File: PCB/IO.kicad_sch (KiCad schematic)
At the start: 39 parts, among them J501 Conn_02x03_Counter_Clockwise, J502 USB_C_Receptacle_USB2.0_16P, J503 Screw_Terminal_01x06, J504 Screw_Terminal_01x04, J505 Conn_01x04, J506 Conn_02x03_Counter_Clockwise, J507 Conn_01x06, J508 VCC, Q1 SL2302S, SW1 SW_Push, SW2 SW_Push

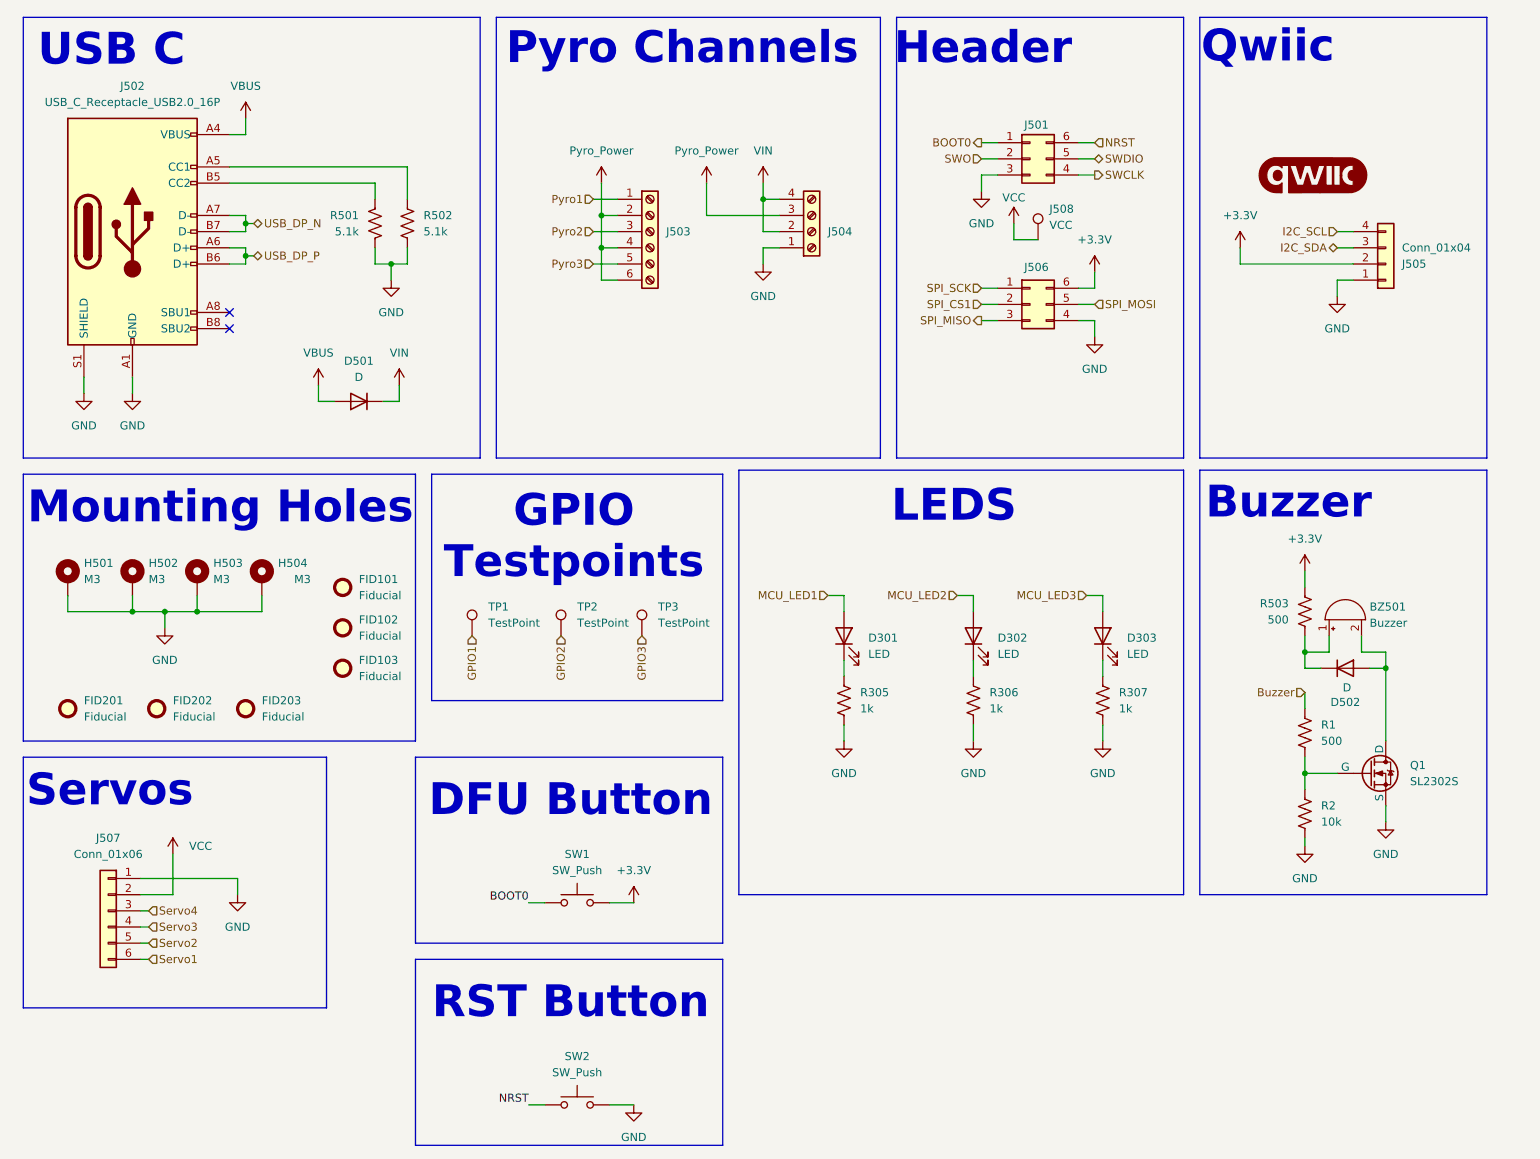
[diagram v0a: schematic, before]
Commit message: - Swapped out 2 LED's for neopixels- Added reverse polarity protection- Replaced Radio module with deticated IC and passives
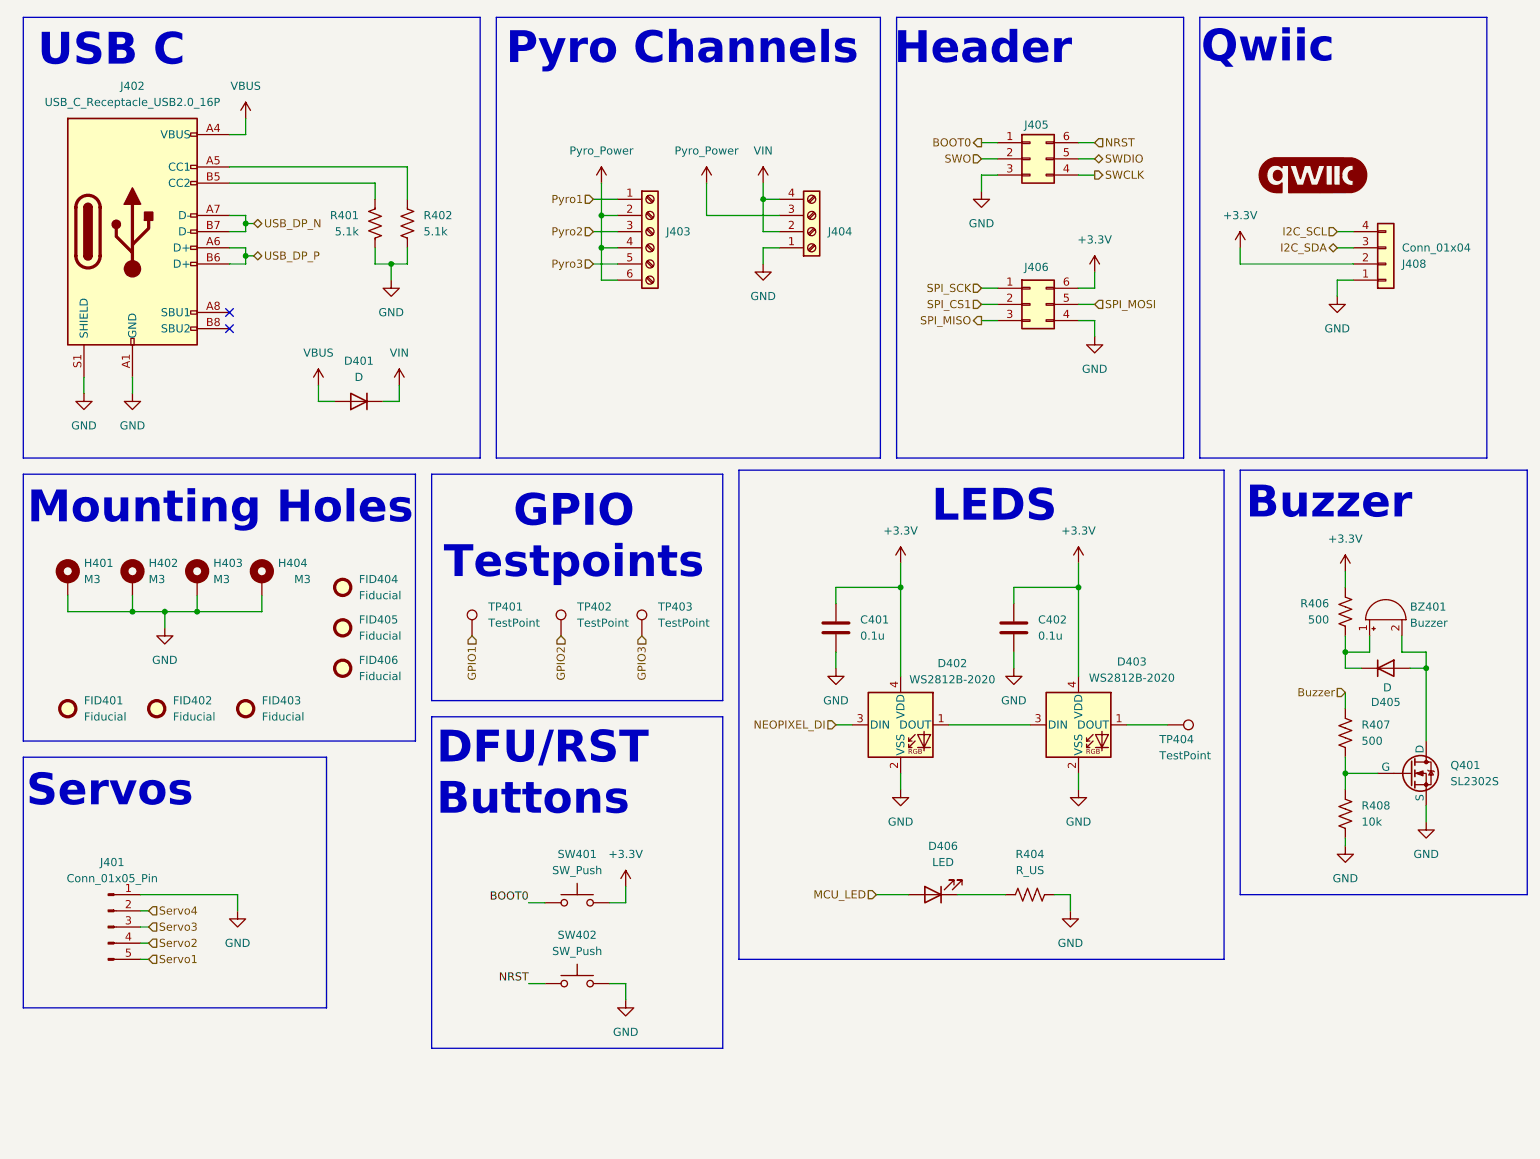
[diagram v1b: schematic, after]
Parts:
- removed D301, D302, D303: LED, LED_SMD:LED_0603_1608Metric_Pad1.05x0.95mm_HandSolder, symbol Device:LED
- removed J507: Conn_01x06, Connector_PinHeader_2.54mm:PinHeader_1x06_P2.54mm_Vertical, symbol Connector_Generic:Conn_01x06
- removed J508: VCC, TestPoint:TestPoint_Pad_1.0x1.0mm, symbol Connector:TestPoint
- removed R305, R306, R307: 1k, Resistor_SMD:R_0603_1608Metric_Pad0.98x0.95mm_HandSolder, symbol Device:R_US
- added C401, C402: 0.1u, Capacitor_SMD:C_0603_1608Metric_Pad1.08x0.95mm_HandSolder, symbol Device:C
- added D402, D403: WS2812B-2020, LED_SMD:LED_WS2812B-2020_PLCC4_2.0x2.0mm, symbol LED:WS2812B-2020
- added D406: LED, LED_SMD:LED_0603_1608Metric_Pad1.05x0.95mm_HandSolder, symbol Device:LED
- added J401: Conn_01x05_Pin, Connector_PinHeader_2.54mm:PinHeader_1x05_P2.54mm_Vertical, symbol Connector:Conn_01x05_Pin
- added R404: R_US, Resistor_SMD:R_0603_1608Metric_Pad0.98x0.95mm_HandSolder, symbol Device:R_US
- added TP404: TestPoint, TestPoint:TestPoint_Pad_D1.5mm, symbol Connector:TestPoint
- renumbered BZ501 to BZ401, D501 to D401, D502 to D405, FID201 to FID401, FID202 to FID402, FID203 to FID403, FID101 to FID404, FID102 to FID405, FID103 to FID406, G501 to G401, H501 to H401, H502 to H402, H503 to H403, H504 to H404, J502 to J402, J503 to J403, J504 to J404, J501 to J405, J506 to J406, J505 to J408, Q1 to Q401, R501 to R401, R502 to R402, R503 to R406, R1 to R407, R2 to R408, SW1 to SW401, SW2 to SW402, TP1 to TP401, TP2 to TP402, TP3 to TP403
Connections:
- net +3.3V: now also C401.1, C402.1, D402.4 (VDD), D403.4 (VDD)
- net GND: now also C401.2, C402.2, D402.2 (VSS), D403.2 (VSS), J401.1 (Pin_1), R404.2
- net Servo1: now also J401.5 (Pin_5)
- net Servo2: now also J401.4 (Pin_4)
- net Servo3: now also J401.3 (Pin_3)
- net Servo4: now also J401.2 (Pin_2)
- new net: D406.1 (K), R404.1
- new net: D402.1 (DOUT), D403.3 (DIN)
- new net: D403.1 (DOUT), TP404.1
- new net MCU_LED: D406.2 (A)
- new net NEOPIXEL_DI: D402.3 (DIN)
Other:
- note added: "DFU/RST Buttons"
- note removed: "DFU Button"
- note removed: "RST Button"
- moved on the sheet: BZ401, D405, Q401, R406, R407, R408, SW402

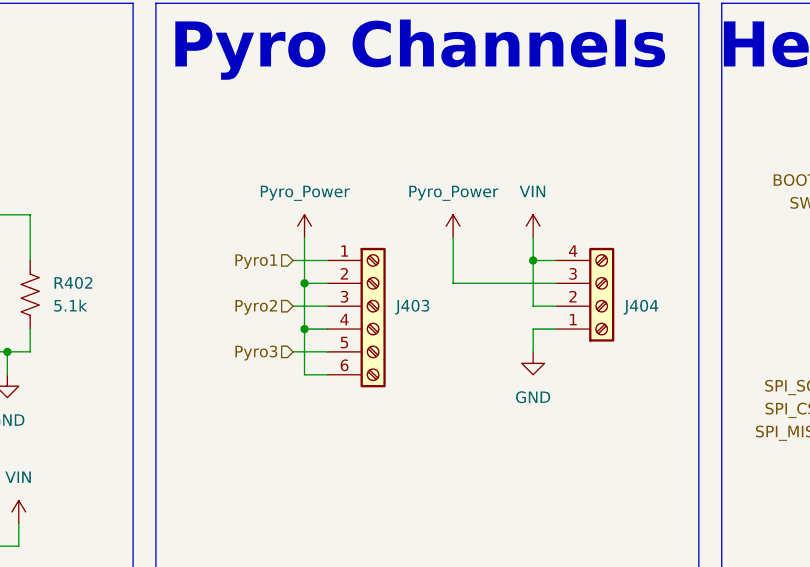
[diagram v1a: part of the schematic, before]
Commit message: Updated PCB to have the new parts (unrouted)
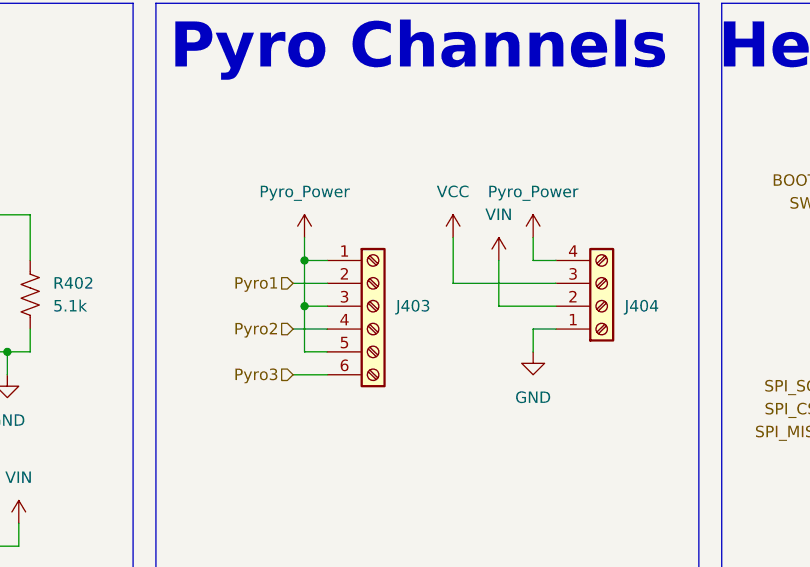
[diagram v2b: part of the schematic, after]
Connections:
- net +3.3V: now also SW401.3, SW401.4; no longer SW401.2
- net BOOT0: now also SW401.2
- net GND: now also SW402.3, SW402.4; no longer SW402.2
- net NRST: now also SW402.2
- net Pyro1: now also J403.2 (Pin_2); no longer J403.1 (Pin_1)
- net Pyro2: now also J403.4 (Pin_4); no longer J403.3 (Pin_3)
- net Pyro3: now also J403.6 (Pin_6); no longer J403.5 (Pin_5)
- net Pyro_Power: now also J403.1 (Pin_1), J403.3 (Pin_3), J403.5 (Pin_5), J404.4 (Pin_4); no longer J403.2 (Pin_2), J403.4 (Pin_4), J403.6 (Pin_6), J404.3 (Pin_3)
- net VIN: no longer J404.4 (Pin_4)
- new net VCC: J404.3 (Pin_3)
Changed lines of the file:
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@@
 	)
 	(junction
-		(at 105.41 50.8)
+		(at 105.41 48.26)
 		(diameter 0)
 		(color 0 0 0 0)
@@
 	)
 	(junction
-		(at 105.41 45.72)
-		(diameter 0)
-		(color 0 0 0 0)
-	)
-	(junction
 		(at 234.95 116.84)
 		(diameter 0)
@@
 	)
 	(junction
-		(at 130.81 43.18)
+		(at 72.39 53.34)
 		(diameter 0)
 		(color 0 0 0 0)
 	)
 	(junction
-		(at 72.39 53.34)
+		(at 105.41 43.18)
 		(diameter 0)
 		(color 0 0 0 0)
@@
 	(wire
 		(pts
-			(xy 104.14 53.34) (xy 107.95 53.34)
-		)
-		(stroke
-			(width 0)
-			(type default)
-		)
-	)
-	(wire
-		(pts
 			(xy 60.96 74.93) (xy 63.5 74.93)
 		)
@@
 	(wire
 		(pts
-			(xy 107.95 55.88) (xy 105.41 55.88)
+			(xy 234.95 114.3) (xy 234.95 116.84)
 		)
 		(stroke
@@
 	(wire
 		(pts
-			(xy 234.95 114.3) (xy 234.95 116.84)
+			(xy 104.14 55.88) (xy 107.95 55.88)
 		)
 		(stroke
@@
 	(wire
 		(pts
-			(xy 133.35 48.26) (xy 130.81 48.26)
+			(xy 220.98 58.42) (xy 220.98 55.88)
 		)
 		(stroke
@@
 	(wire
 		(pts
-			(xy 220.98 58.42) (xy 220.98 55.88)
+			(xy 165.1 39.37) (xy 167.64 39.37)
 		)
 		(stroke
@@
 	(wire
 		(pts
-			(xy 165.1 39.37) (xy 167.64 39.37)
+			(xy 21.59 107.95) (xy 21.59 105.41)
 		)
 		(stroke
@@
 	(wire
 		(pts
-			(xy 21.59 107.95) (xy 21.59 105.41)
+			(xy 142.24 104.14) (xy 152.4 104.14)
 		)
 		(stroke
@@
 	(wire
 		(pts
-			(xy 142.24 104.14) (xy 152.4 104.14)
+			(xy 182.88 36.83) (xy 180.34 36.83)
 		)
 		(stroke
@@
 	(wire
 		(pts
-			(xy 182.88 36.83) (xy 180.34 36.83)
+			(xy 105.41 40.64) (xy 105.41 43.18)
 		)
 		(stroke
@@
 	(wire
 		(pts
-			(xy 105.41 50.8) (xy 105.41 45.72)
+			(xy 127 48.26) (xy 133.35 48.26)
 		)
 		(stroke
@@
 	(wire
 		(pts
-			(xy 105.41 55.88) (xy 105.41 50.8)
+			(xy 107.95 53.34) (xy 105.41 53.34)
 		)
 		(stroke
@@
 	(wire
 		(pts
-			(xy 130.81 48.26) (xy 130.81 43.18)
+			(xy 142.24 104.14) (xy 142.24 106.68)
 		)
 		(stroke
@@
 	(wire
 		(pts
-			(xy 142.24 104.14) (xy 142.24 106.68)
+			(xy 222.25 133.35) (xy 222.25 135.89)
 		)
 		(stroke
@@
 	(wire
 		(pts
-			(xy 222.25 133.35) (xy 222.25 135.89)
+			(xy 72.39 55.88) (xy 72.39 53.34)
 		)
 		(stroke
@@
 	(wire
 		(pts
-			(xy 72.39 55.88) (xy 72.39 53.34)
+			(xy 105.41 48.26) (xy 105.41 53.34)
 		)
 		(stroke
@@
 	(wire
 		(pts
-			(xy 104.14 43.18) (xy 107.95 43.18)
-		)
-		(stroke
-			(width 0)
-			(type default)
-		)
-	)
-	(wire
-		(pts
 			(xy 222.25 144.78) (xy 222.25 143.51)
 		)
@@
 	(wire
 		(pts
-			(xy 105.41 45.72) (xy 107.95 45.72)
+			(xy 105.41 43.18) (xy 107.95 43.18)
 		)
 		(stroke
@@
 	(wire
 		(pts
+			(xy 105.41 48.26) (xy 107.95 48.26)
+		)
+		(stroke
+			(width 0)
+			(type default)
+		)
+	)
+	(wire
+		(pts
 			(xy 36.83 107.95) (xy 41.91 107.95)
 		)
@@
 	(wire
 		(pts
-			(xy 105.41 45.72) (xy 105.41 40.64)
+			(xy 142.24 125.73) (xy 144.78 125.73)
 		)
 		(stroke
@@
 	(wire
 		(pts
-			(xy 142.24 125.73) (xy 144.78 125.73)
+			(xy 121.92 45.72) (xy 133.35 45.72)
 		)
 		(stroke
@@
 	(wire
 		(pts
-			(xy 121.92 45.72) (xy 133.35 45.72)
+			(xy 104.14 50.8) (xy 107.95 50.8)
 		)
 		(stroke
@@
 	(wire
 		(pts
-			(xy 104.14 48.26) (xy 107.95 48.26)
+			(xy 127 43.18) (xy 127 48.26)
 		)
 		(stroke
@@
 	(wire
 		(pts
-			(xy 105.41 50.8) (xy 107.95 50.8)
-		)
-		(stroke
-			(width 0)
-			(type default)
-		)
-	)
-	(wire
-		(pts
 			(xy 180.34 62.23) (xy 182.88 62.23)
 		)
@@
 	(wire
 		(pts
+			(xy 104.14 45.72) (xy 107.95 45.72)
+		)
+		(stroke
+			(width 0)
+			(type default)
+		)
+	)
+	(wire
+		(pts
+			(xy 105.41 43.18) (xy 105.41 48.26)
+		)
+		(stroke
+			(width 0)
+			(type default)
+		)
+	)
+	(wire
+		(pts
 			(xy 33.02 162.56) (xy 34.29 162.56)
 		)
@@
 		)
 	)
-	(hierarchical_label "Pyro2"
-		(shape input)
-		(at 104.14 48.26 180)
-		(effects
-			(font
-				(size 1.27 1.27)
-			)
-			(justify right)
-		)
-	)
 	(hierarchical_label "GPIO2"
 		(shape input)
@@
 		)
 	)
-	(hierarchical_label "Pyro1"
+	(hierarchical_label "Pyro2"
 		(shape input)
-		(at 104.14 43.18 180)
+		(at 104.14 50.8 180)
 		(effects
 			(font
@@
 		)
 	)
+	(hierarchical_label "Pyro1"
+		(shape input)
+		(at 104.14 45.72 180)
+		(effects
+			(font
+				(size 1.27 1.27)
+			)
+			(justify right)
+		)
+	)
 	(hierarchical_label "BOOT0"
 		(shape output)
@@
 		)
 	)
+	(hierarchical_label "Pyro3"
+		(shape input)
+		(at 104.14 55.88 180)
+		(effects
+			(font
+				(size 1.27 1.27)
+			)
+			(justify right)
+		)
+	)
 	(hierarchical_label "SWCLK"
 		(shape output)
@@
 		)
 	)
-	(hierarchical_label "Pyro3"
-		(shape input)
-		(at 104.14 53.34 180)
-		(effects
-			(font
-				(size 1.27 1.27)
-			)
-			(justify right)
-		)
-	)
 	(symbol
 		(lib_id "Connector_Generic:Conn_02x03_Counter_Clockwise")
@@
 			)
 		)
-		(property "Value" "Pyro_Power"
+		(property "Value" "VCC"
 			(at 121.92 35.56 0)
 			(show_name no)
@@
 			)
 		)
-		(property "Value" "VIN"
+		(property "Value" "Pyro_Power"
 			(at 130.81 35.56 0)
 			(show_name no)
@@
 	)
 	(symbol
+		(lib_id "power:VBUS")
+		(at 127 43.18 0)
+		(unit 1)
+		(body_style 1)
+		(exclude_from_sim no)
+		(in_bom yes)
+		(on_board yes)
+		(in_pos_files yes)
+		(dnp no)
+		(fields_autoplaced yes)
+		(property "Reference" "#PWR0429"
+			(at 127 46.99 0)
+			(hide yes)
+			(show_name no)
+			(do_not_autoplace no)
+			(effects
+				(font
+					(size 1.27 1.27)
+				)
+			)
+		)
+		(property "Value" "VIN"
+			(at 127 38.1 0)
+			(show_name no)
+			(do_not_autoplace no)
+			(effects
+				(font
+					(size 1.27 1.27)
+				)
+			)
+		)
+		(property "Footprint" ""
+			(at 127 43.18 0)
+			(hide yes)
+			(show_name no)
+			(do_not_autoplace no)
+			(effects
+				(font
+					(size 1.27 1.27)
+				)
+			)
+		)
+		(property "Datasheet" ""
+			(at 127 43.18 0)
+			(hide yes)
+			(show_name no)
+			(do_not_autoplace no)
+			(effects
+				(font
+					(size 1.27 1.27)
+				)
+			)
+		)
+		(property "Description" "Power symbol creates a global label with name \"VBUS\""
+			(at 127 43.18 0)
+			(hide yes)
+			(show_name no)
+			(do_not_autoplace no)
+			(effects
+				(font
+					(size 1.27 1.27)
+				)
+			)
+		)
+		(pin "1"
+		)
+		(instances
+			(project "Flight Computer"
+				(path "/4254ccd1-49f4-4fe6-9bf7-ccb200d73af4/0a0b3d01-7422-42e0-b725-ff9e85b891ec"
+					(reference "#PWR0429")
+					(unit 1)
+				)
+			)
+		)
+	)
+	(symbol
 		(lib_id "Mechanical:Fiducial")
 		(at 21.59 123.19 0)
@@
 	)
 	(symbol
+		(lib_name "SW_Push_1")
 		(lib_id "Switch:SW_Push")
 		(at 101.6 153.67 0)
@@
 		(pin "1"
 		)
+		(pin "4"
+		)
+		(pin "3"
+		)
 		(instances
 			(project "Flight Computer"
@@
 		(pin "1"
 		)
+		(pin "3"
+		)
+		(pin "4"
+		)
 		(instances

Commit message: Routed PCB
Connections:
- net SPI_CS1: now also J406.5 (Pin_5); no longer J406.2 (Pin_2)
- net SPI_MISO: now also J406.1 (Pin_1); no longer J406.3 (Pin_3)
- net SPI_MOSI: now also J406.3 (Pin_3); no longer J406.5 (Pin_5)
- net SPI_SCK: now also J406.2 (Pin_2); no longer J406.1 (Pin_1)
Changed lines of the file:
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@@
 	(hierarchical_label "SPI_MOSI"
 		(shape input)
-		(at 182.88 59.69 0)
+		(at 165.1 62.23 180)
 		(effects
 			(font
 				(size 1.27 1.27)
 			)
-			(justify left)
+			(justify right)
 		)
 	)
@@
 	(hierarchical_label "SPI_SCK"
 		(shape input)
-		(at 165.1 57.15 180)
+		(at 165.1 59.69 180)
 		(effects
 			(font
@@
 	(hierarchical_label "SPI_CS1"
 		(shape input)
-		(at 165.1 59.69 180)
+		(at 182.88 59.69 0)
 		(effects
 			(font
 				(size 1.27 1.27)
 			)
-			(justify right)
+			(justify left)
 		)
 	)
@@
 	(hierarchical_label "SPI_MISO"
 		(shape output)
-		(at 165.1 62.23 180)
+		(at 165.1 57.15 180)
 		(effects
 			(font

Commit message: Updated BOM
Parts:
- C401, C402: value 0.1u -> .1u
- R404: value R_US -> 1k
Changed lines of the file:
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@@
 			)
 		)
-		(property "Value" "0.1u"
+		(property "Value" ".1u"
 			(at 146.05 111.7599 0)
 			(show_name no)
@@
 			)
 		)
-		(property "Value" "R_US"
+		(property "Value" "1k"
 			(at 172.72 148.59 90)
 			(show_name no)
@@
 			)
 		)
-		(property "Value" "0.1u"
+		(property "Value" ".1u"
 			(at 173.99 111.7599 0)
 			(show_name no)

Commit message: Added logo to project files. Added courtyard to logo. Added Componet Pos to jobset
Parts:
- FID401, FID402, FID403, FID404, FID405, FID406: footprint Fiducial:Fiducial_0.75mm_Mask1.5mm -> Fiducial:Fiducial_1mm_Mask2mm
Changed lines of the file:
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@@
 			)
 		)
-		(property "Footprint" "Fiducial:Fiducial_0.75mm_Mask1.5mm"
+		(property "Footprint" "Fiducial:Fiducial_1mm_Mask2mm"
 			(at 64.77 116.84 0)
 			(hide yes)
@@
 			)
 		)
-		(property "Footprint" "Fiducial:Fiducial_0.75mm_Mask1.5mm"
+		(property "Footprint" "Fiducial:Fiducial_1mm_Mask2mm"
 			(at 64.77 104.14 0)
 			(hide yes)
@@
 			)
 		)
-		(property "Footprint" "Fiducial:Fiducial_0.75mm_Mask1.5mm"
+		(property "Footprint" "Fiducial:Fiducial_1mm_Mask2mm"
 			(at 35.56 123.19 0)
 			(hide yes)
@@
 			)
 		)
-		(property "Footprint" "Fiducial:Fiducial_0.75mm_Mask1.5mm"
+		(property "Footprint" "Fiducial:Fiducial_1mm_Mask2mm"
 			(at 49.53 123.19 0)
 			(hide yes)
@@
 			)
 		)
-		(property "Footprint" "Fiducial:Fiducial_0.75mm_Mask1.5mm"
+		(property "Footprint" "Fiducial:Fiducial_1mm_Mask2mm"
 			(at 64.77 110.49 0)
 			(hide yes)
@@
 			)
 		)
-		(property "Footprint" "Fiducial:Fiducial_0.75mm_Mask1.5mm"
+		(property "Footprint" "Fiducial:Fiducial_1mm_Mask2mm"
 			(at 21.59 123.19 0)
 			(hide yes)
